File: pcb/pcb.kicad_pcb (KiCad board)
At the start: 4 copper layers, 48.3 x 68.5 mm, 52 parts, among them J1 Conn_02x09_Odd_Even, J10 Conn_01x04, J11 Conn_01x02, J12 Conn_01x02, J2 Conn_02x09_Odd_Even, J3 Conn_02x09_Odd_Even, J4 Conn_02x09_Odd_Even, J5 Jack-DC, J6 Conn_01x04, J7 Conn_01x05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

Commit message: uart
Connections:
- J7 pad 3: Net-(J7-Pad3) -> /p2f_3v3
- J7 pad 4: /print_3v3 -> /f2p_3v3
- X1 pad 21: Net-(X1-Pad21) -> /f2p_3v3
- X1 pad 22: /print_3v3 -> /dtr_3v3
- X1 pad 23: /dtr_3v3 -> /p2f_3v3
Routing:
- net /f2p_3v3: track 0.00 -> 41.7 mm
- net /print_3v3: track 36.8 -> 0.00 mm
- net /p2f_3v3: track 0.00 -> 34.2 mm
- net /dtr_3v3: track 27.9 -> 31.7 mm

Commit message: pull down
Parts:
- added R7: 33k, Resistor_SMD:R_0402_1005Metric, B.Cu at (107.5, 103.6)
- added R8: 33k, Resistor_SMD:R_0402_1005Metric, B.Cu at (107.5, 101.0)
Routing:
- net GND: track 451.3 -> 460.0 mm
- net /dtr_3v3: track 31.7 -> 33.7 mm
- net /p2f_3v3: track 34.2 -> 36.2 mm

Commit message: pcb adjust
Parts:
- removed C15, C17: 100n, Capacitor_SMD:C_0402_1005Metric
- removed RV2: R_POT, Potentiometer_SMD:Potentiometer_Vishay_TS53YL_Vertical
- removed U7: TXS0102, kicad-lib:TI-R-PDSO-G8
- added R10: 1.02k, 0.5%, Resistor_SMD:R_0603_1608Metric, B.Cu at (148.1, 131.8)
- added R11: 5.36k, 0.5%, Resistor_SMD:R_0603_1608Metric, F.Cu at (118.9, 117.6)
- added R12: 1.02k, 0.5%, Resistor_SMD:R_0603_1608Metric, F.Cu at (119.6, 119.9)
- added R9: 2.15k, 0.5%, Resistor_SMD:R_0603_1608Metric, B.Cu at (142.0, 132.2)
- J10: value Conn_01x04 -> Conn_01x05; footprint Connector_PinHeader_2.54mm:PinHeader_1x04_P2.54mm_Vertical -> Connector_PinHeader_2.54mm:PinHeader_1x05_P2.54mm_Vertical
- J5: footprint Connector_BarrelJack:BarrelJack_CUI_PJ-063AH_Horizontal -> b1:KLDX-0202
- RV1: value R_POT -> 1k
- moved Y2 14.1 mm to (122.1, 130.0), turned to 270 degrees
- moved J6 7.93 mm to (111.2, 130.7), turned to 270 degrees
- moved J10 7.62 mm to (119.4, 98.6), turned to 0 degrees
- moved C2 3.70 mm to (121.3, 135.5), turned to 0 degrees
- moved Y1 1.91 mm to (112.9, 87.0)
- moved C1 1.40 mm to (121.1, 140.3), turned to 270 degrees
- moved J5 0.84 mm to (112.2, 137.9), turned to 90 degrees
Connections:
- J10 pad 1: /+5V -> /scl_3v3
- J10 pad 2: GND -> /sda_3v3
- J10 pad 3: /sda_5v -> GND
- J10 pad 4: /scl_5v -> /+5V
- RV1 pad 1: GND -> Net-(R10-Pad1)
- RV1 pad 3: /VADJ1 -> Net-(R9-Pad2)
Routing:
- net /+5V: track 37.7 -> 8.89 mm, vias 1 -> 0
- net /sda_5v: track 19.9 -> 0.00 mm
- net /scl_5v: track 18.1 -> 0.00 mm
- net /+3V3: track 56.5 -> 43.0 mm, vias 0 -> 1
- net /VADJ1: track 34.3 -> 24.7 mm
- net /f2p_3v3: track 41.7 -> 32.3 mm
- net /sda_3v3: track 21.3 -> 30.2 mm
- net /dtr_3v3: track 33.7 -> 26.6 mm
- net GND: track 460.0 -> 453.6 mm, vias 16 -> 18
- net /VADJ2: track 34.1 -> 29.1 mm
- net /p2f_3v3: track 36.2 -> 31.6 mm
- net /VIN0: track 5.50 -> 9.98 mm
- net Net-(R10-Pad1): track 0.00 -> 3.47 mm, vias 0 -> 1
- net Net-(R9-Pad2): track 0.00 -> 3.36 mm, vias 0 -> 1
- net /VIN: track 85.8 -> 83.0 mm
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
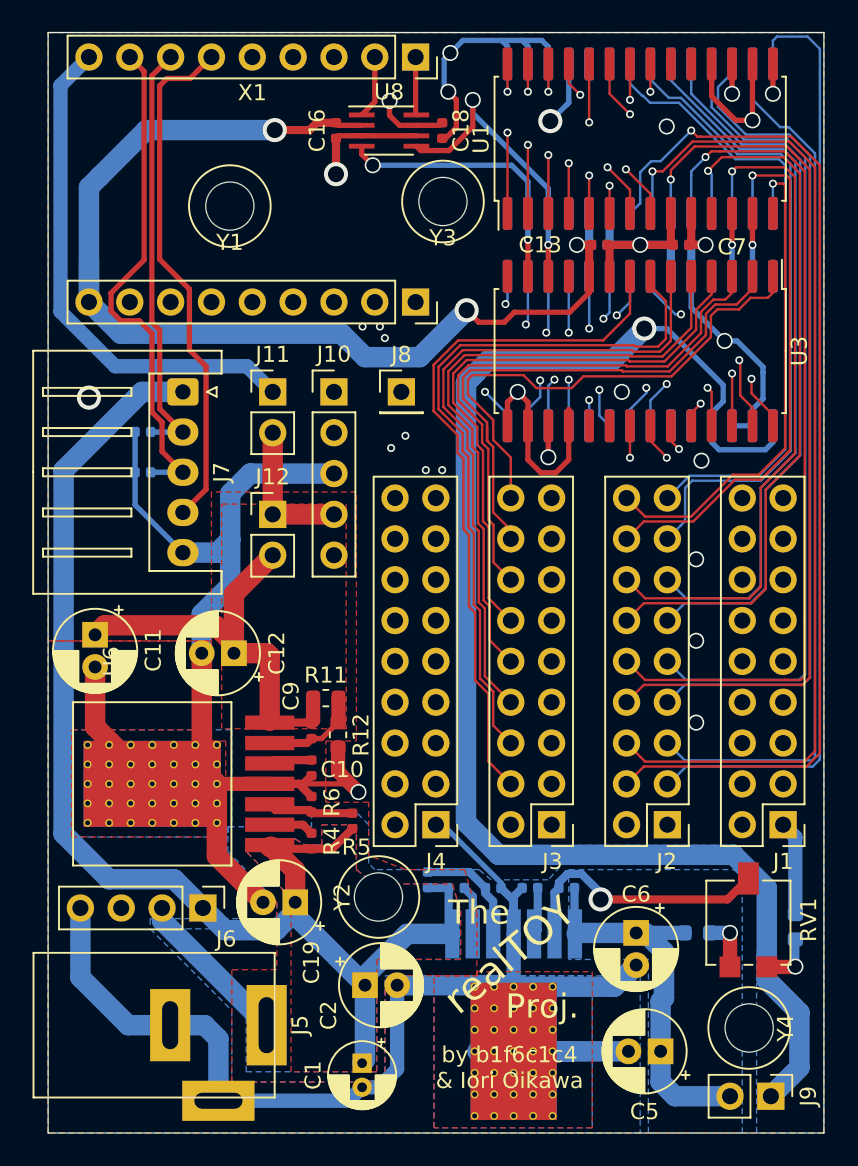
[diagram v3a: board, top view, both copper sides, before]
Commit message: no in1 routing
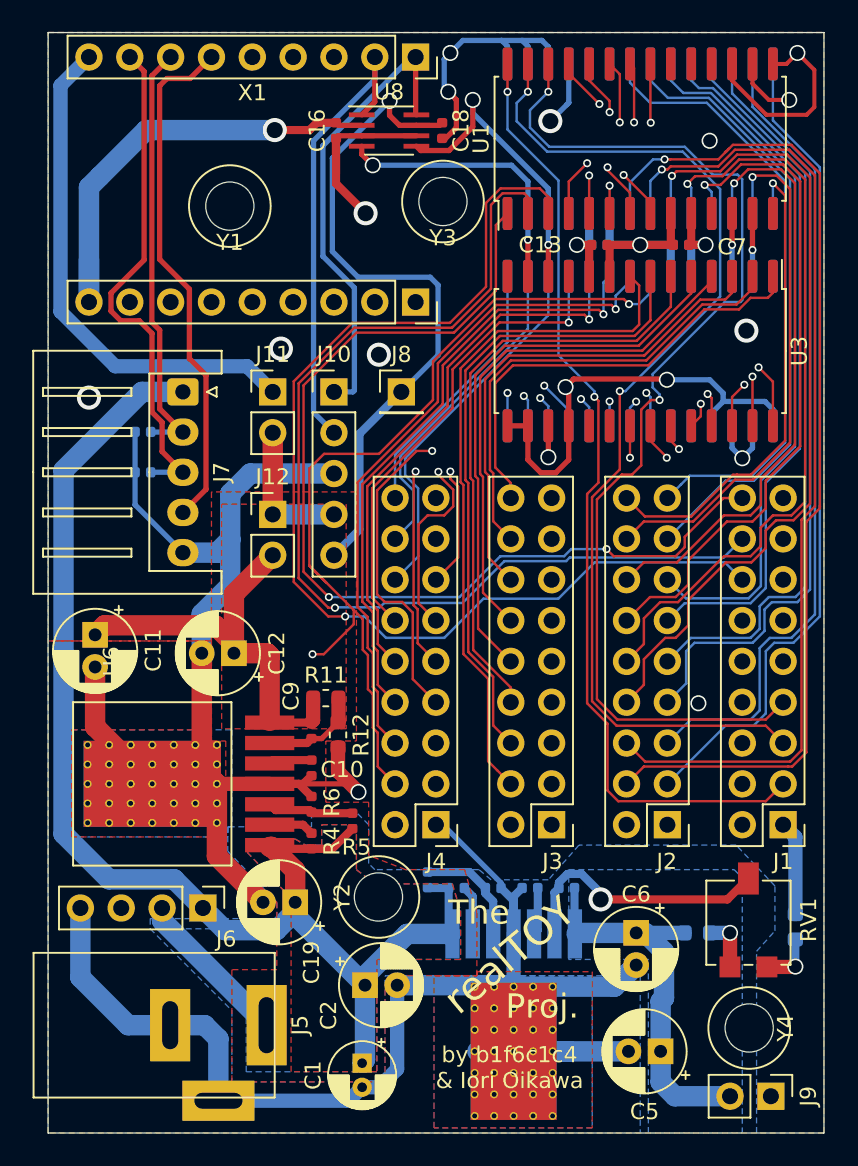
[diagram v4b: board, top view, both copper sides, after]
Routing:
- net GND: track 453.6 -> 265.2 mm, vias 18 -> 14
- net Net-(J1-Pad14): track 43.6 -> 69.3 mm
- net Net-(J1-Pad16): track 43.4 -> 65.6 mm
- net Net-(J1-Pad18): track 43.0 -> 62.9 mm, vias 1 -> 2
- net Net-(J4-Pad6): track 59.0 -> 41.8 mm
- net Net-(J4-Pad10): track 49.1 -> 34.0 mm
- net Net-(J4-Pad12): track 44.5 -> 29.6 mm
- net Net-(J4-Pad8): track 52.6 -> 37.9 mm
- net Net-(J4-Pad14): track 36.8 -> 23.5 mm, vias 2 -> 0
- net Net-(J4-Pad16): track 30.7 -> 20.4 mm, vias 2 -> 0
- net Net-(J1-Pad7): track 59.4 -> 69.2 mm, vias 1 -> 2
- net Net-(J1-Pad3): track 68.6 -> 60.0 mm, vias 1 -> 2
- net Net-(J4-Pad18): track 25.0 -> 16.7 mm, vias 2 -> 0
- net Net-(J2-Pad3): track 59.2 -> 51.6 mm
- net Net-(J2-Pad10): track 53.9 -> 47.3 mm
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
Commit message: many pcb changes
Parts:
- moved R5 1.14 mm to (119.4, 125.2)
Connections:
- J4 pad 4: /btn_power_o -> Net-(J4-Pad4)
- J6 pad 3: /btn_power_o -> VDD
- U4 pad 8: /btn_power_o -> Net-(J4-Pad4)
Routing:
- net GND: track 265.2 -> 575.2 mm, vias 14 -> 19
- net /btn_power_o: track 82.1 -> 0.00 mm, vias 2 -> 0
- net Net-(J4-Pad4): track 0.00 -> 46.0 mm, vias 0 -> 1
- net VDD: track 207.6 -> 235.4 mm
- net Net-(J2-Pad17): track 38.4 -> 42.4 mm
- net Net-(J2-Pad8): track 51.4 -> 54.1 mm
- net /+3V3: track 44.7 -> 42.3 mm
- net Net-(J2-Pad10): track 47.3 -> 49.7 mm
- net Net-(J1-Pad9): track 49.4 -> 51.6 mm
- net Net-(J1-Pad13): track 42.6 -> 44.8 mm
- net Net-(J1-Pad11): track 45.9 -> 48.1 mm
- net Net-(J1-Pad15): track 38.3 -> 40.5 mm
- net Net-(J1-Pad17): track 33.5 -> 35.5 mm
- net /sda: track 36.7 -> 38.7 mm
- net Net-(J2-Pad15): track 38.8 -> 40.5 mm
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
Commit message: tune
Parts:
- added C15: 100n, Capacitor_SMD:C_0402_1005Metric, B.Cu at (125.0, 134.0)
- added C17: 100n, Capacitor_SMD:C_0402_1005Metric, F.Cu at (114.5, 128.4)
- moved C19 0.97 mm to (117.9, 130.7)
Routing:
- net GND: track 575.2 -> 582.0 mm, vias 19 -> 26
- net /VIN: track 82.8 -> 87.5 mm
- net /sda: track 38.7 -> 36.0 mm
- net Net-(J1-Pad6): track 49.8 -> 47.7 mm
- net Net-(J1-Pad8): track 48.3 -> 46.9 mm
- net Net-(J1-Pad10): track 48.1 -> 46.7 mm
- net Net-(J1-Pad7): track 70.0 -> 71.2 mm
- net Net-(J1-Pad5): track 67.2 -> 68.2 mm
- net Net-(J1-Pad4): track 50.5 -> 49.6 mm
- net Net-(J3-Pad4): track 42.6 -> 41.7 mm
- net Net-(J3-Pad6): track 39.9 -> 39.0 mm
- net Net-(J3-Pad8): track 37.6 -> 36.7 mm
- net Net-(J1-Pad13): track 44.8 -> 44.0 mm
- net Net-(J1-Pad15): track 40.5 -> 39.7 mm
- net Net-(J1-Pad12): track 44.0 -> 43.4 mm
